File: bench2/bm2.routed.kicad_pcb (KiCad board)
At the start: 2 copper layers, 50.8 x 22.9 mm, 18 parts, among them IC1 PCF8523T, SW1 KMR2, X4 microsd, Y1 32khz

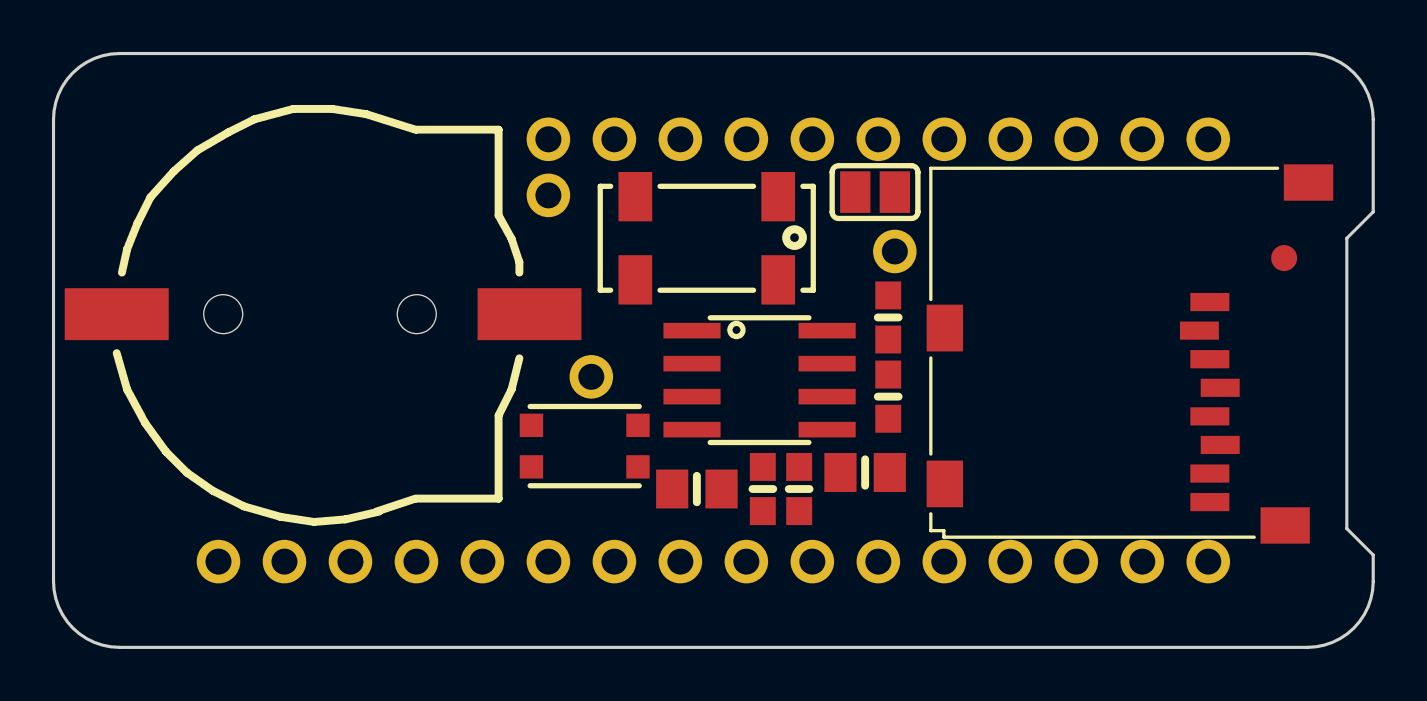
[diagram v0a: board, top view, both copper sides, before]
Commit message: prepare to add pad shape
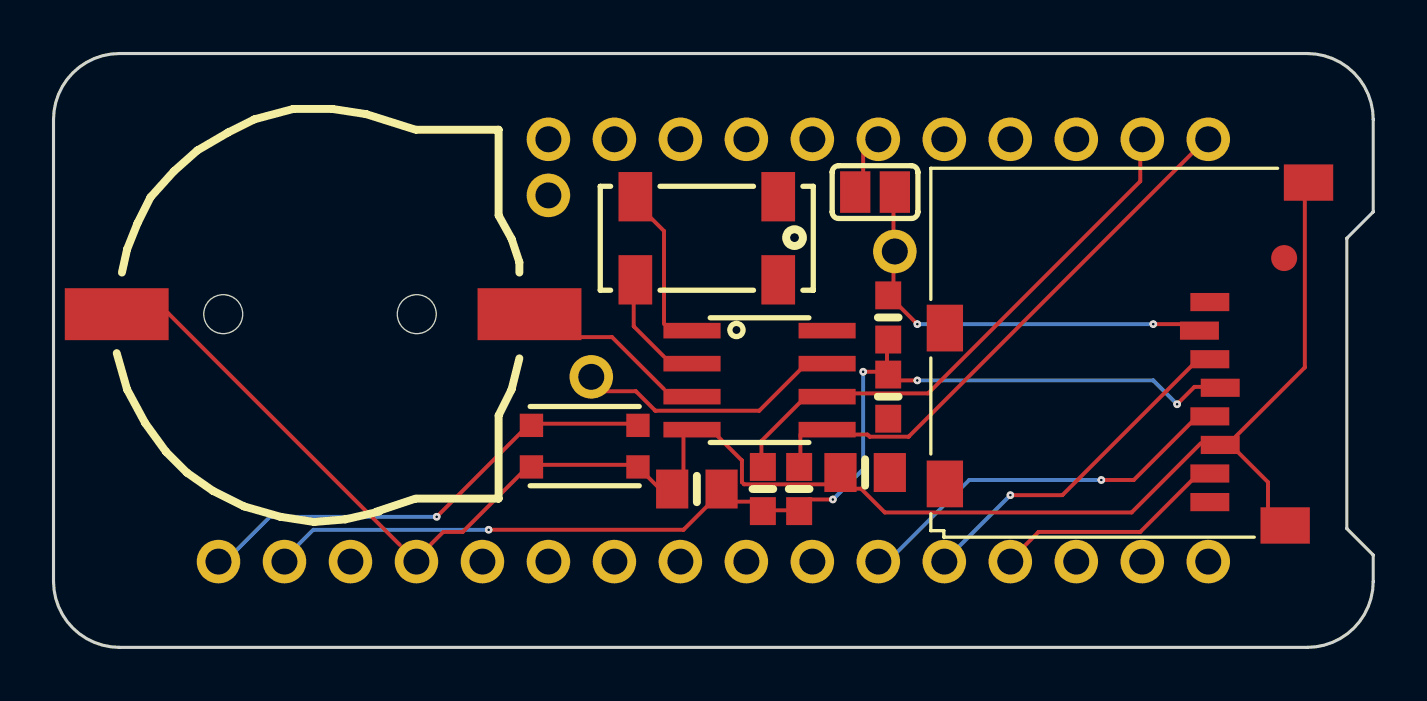
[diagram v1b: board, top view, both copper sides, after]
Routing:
- net GND: track 0.00 -> 56.9 mm
- net +3V3: track 0.00 -> 38.0 mm, vias 0 -> 5
- net SDA: track 0.00 -> 18.5 mm
- net SCL: track 0.00 -> 18.3 mm
- net RESET: track 0.00 -> 16.7 mm, vias 0 -> 1
- net SCK: track 0.00 -> 13.6 mm, vias 0 -> 1
- net SD_CS: track 0.00 -> 13.0 mm, vias 0 -> 2
- net MOSI: track 0.00 -> 11.9 mm, vias 0 -> 1
- net INT1: track 0.00 -> 8.47 mm
- net MISO: track 0.00 -> 7.57 mm
- net N$7: track 0.00 -> 4.41 mm
- net CR1220: track 0.00 -> 4.16 mm
- net N$8: track 0.00 -> 2.65 mm
- net CS: track 0.00 -> 0.75 mm

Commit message: optimized via cost
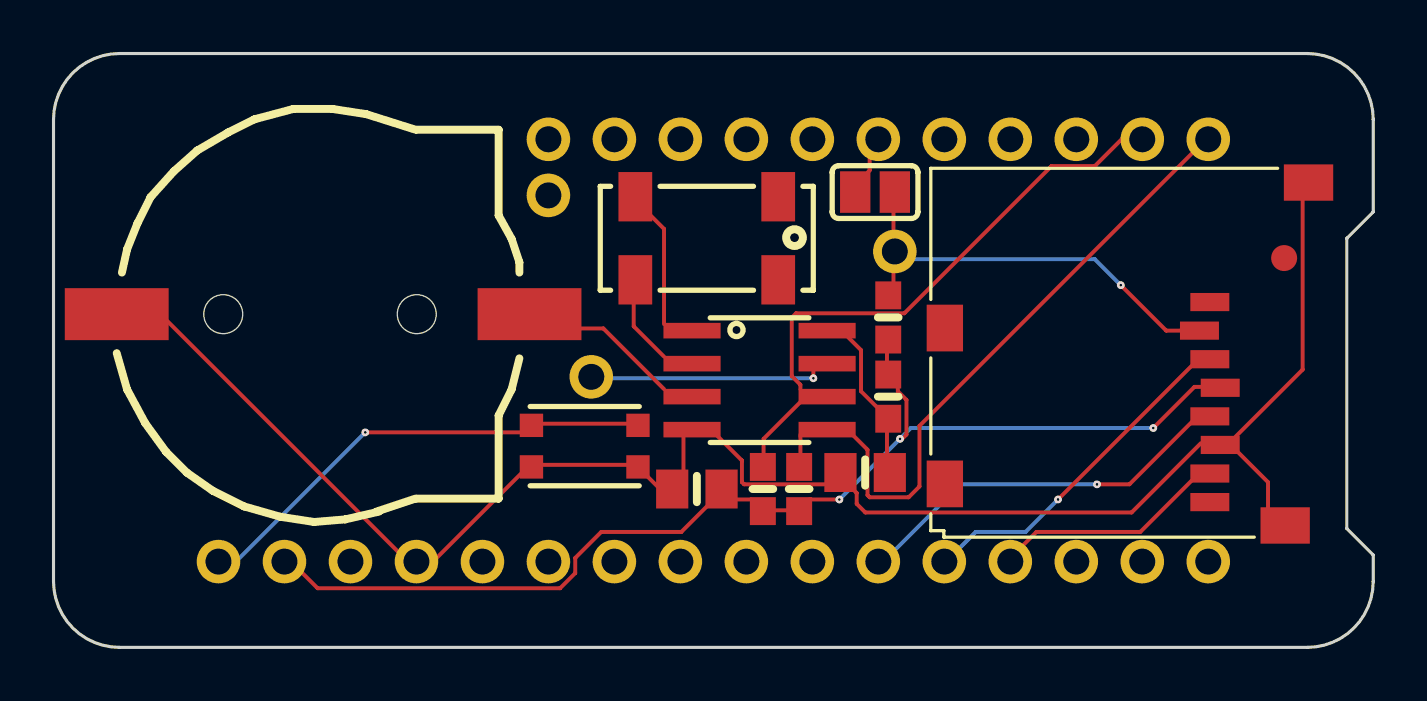
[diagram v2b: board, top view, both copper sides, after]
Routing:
- net SDA: track 18.5 -> 22.8 mm
- net G: track 0.00 -> 4.12 mm
- net SCL: track 18.3 -> 21.1 mm
- net +3V3: track 38.0 -> 38.7 mm, vias 5 -> 3
- net INT1: track 8.47 -> 8.25 mm, vias 0 -> 1
- net SD_CS: track 13.0 -> 12.8 mm, vias 2 -> 1
